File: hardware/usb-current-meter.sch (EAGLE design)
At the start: 28 parts, among them IC2 OPA2234U, U1 ATTINY45, X1 MC2, X3 USB-A-H

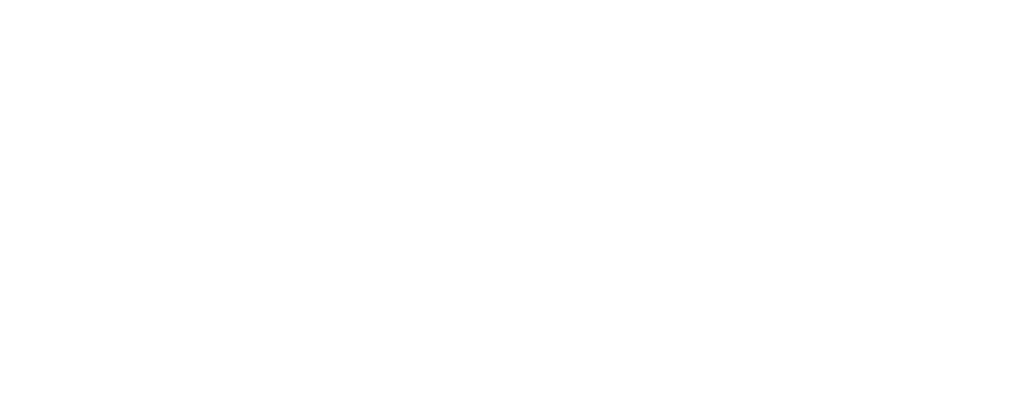
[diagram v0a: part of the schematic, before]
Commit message: hardware: add license, silkscreen
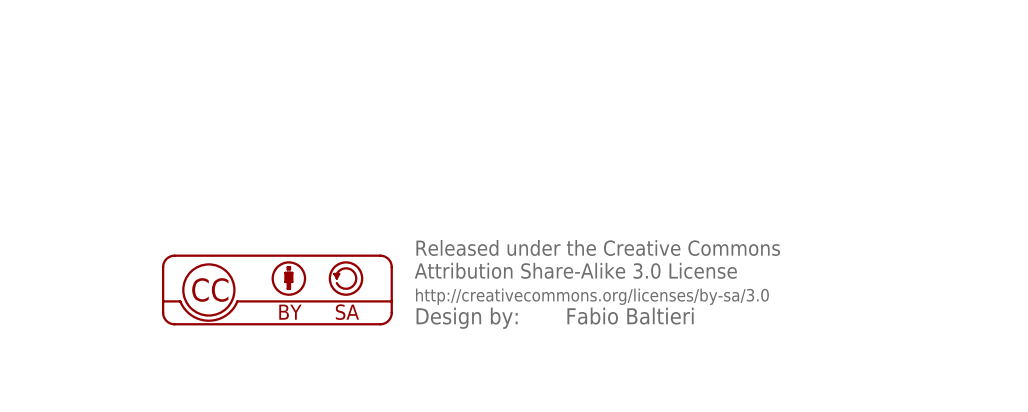
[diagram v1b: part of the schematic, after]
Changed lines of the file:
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@@
 <grid distance="0.1" unitdist="inch" unit="inch" style="lines" multiple="1" display="no" altdistance="0.01" altunitdist="inch" altunit="inch"/>
 <layers>
-<layer number="1" name="Top" color="4" fill="1" visible="yes" active="no"/>
-<layer number="16" name="Bottom" color="1" fill="1" visible="yes" active="no"/>
-<layer number="17" name="Pads" color="2" fill="1" visible="yes" active="no"/>
-<layer number="18" name="Vias" color="2" fill="1" visible="yes" active="no"/>
-<layer number="19" name="Unrouted" color="6" fill="1" visible="yes" active="no"/>
-<layer number="20" name="Dimension" color="15" fill="1" visible="yes" active="no"/>
-<layer number="21" name="tPlace" color="7" fill="1" visible="yes" active="no"/>
-<layer number="22" name="bPlace" color="7" fill="1" visible="yes" active="no"/>
-<layer number="23" name="tOrigins" color="15" fill="1" visible="yes" active="no"/>
-<layer number="24" name="bOrigins" color="15" fill="1" visible="yes" active="no"/>
-<layer number="25" name="tNames" color="7" fill="1" visible="yes" active="no"/>
-<layer number="26" name="bNames" color="7" fill="1" visible="yes" active="no"/>
-<layer number="27" name="tValues" color="7" fill="1" visible="yes" active="no"/>
-<layer number="28" name="bValues" color="7" fill="1" visible="yes" active="no"/>
+<layer number="1" name="Top" color="4" fill="1" visible="no" active="no"/>
+<layer number="16" name="Bottom" color="1" fill="1" visible="no" active="no"/>
+<layer number="17" name="Pads" color="2" fill="1" visible="no" active="no"/>
+<layer number="18" name="Vias" color="2" fill="1" visible="no" active="no"/>
+<layer number="19" name="Unrouted" color="6" fill="1" visible="no" active="no"/>
+<layer number="20" name="Dimension" color="15" fill="1" visible="no" active="no"/>
+<layer number="21" name="tPlace" color="7" fill="1" visible="no" active="no"/>
+<layer number="22" name="bPlace" color="7" fill="1" visible="no" active="no"/>
+<layer number="23" name="tOrigins" color="15" fill="1" visible="no" active="no"/>
+<layer number="24" name="bOrigins" color="15" fill="1" visible="no" active="no"/>
+<layer number="25" name="tNames" color="7" fill="1" visible="no" active="no"/>
+<layer number="26" name="bNames" color="7" fill="1" visible="no" active="no"/>
+<layer number="27" name="tValues" color="7" fill="1" visible="no" active="no"/>
+<layer number="28" name="bValues" color="7" fill="1" visible="no" active="no"/>
 <layer number="29" name="tStop" color="7" fill="3" visible="no" active="no"/>
 <layer number="30" name="bStop" color="7" fill="6" visible="no" active="no"/>
@@
 <layer number="35" name="tGlue" color="7" fill="4" visible="no" active="no"/>
 <layer number="36" name="bGlue" color="7" fill="5" visible="no" active="no"/>
-<layer number="37" name="tTest" color="7" fill="1" visible="yes" active="no"/>
-<layer number="38" name="bTest" color="7" fill="1" visible="yes" active="no"/>
+<layer number="37" name="tTest" color="7" fill="1" visible="no" active="no"/>
+<layer number="38" name="bTest" color="7" fill="1" visible="no" active="no"/>
 <layer number="39" name="tKeepout" color="4" fill="11" visible="no" active="no"/>
 <layer number="40" name="bKeepout" color="1" fill="11" visible="no" active="no"/>
@@
 <layer number="44" name="Drills" color="7" fill="1" visible="no" active="no"/>
 <layer number="45" name="Holes" color="7" fill="1" visible="no" active="no"/>
-<layer number="46" name="Milling" color="3" fill="1" visible="yes" active="no"/>
-<layer number="47" name="Measures" color="7" fill="1" visible="yes" active="no"/>
-<layer number="48" name="Document" color="7" fill="1" visible="yes" active="no"/>
-<layer number="49" name="Reference" color="7" fill="1" visible="yes" active="no"/>
-<layer number="50" name="dxf" color="7" fill="1" visible="yes" active="no"/>
-<layer number="51" name="tDocu" color="7" fill="1" visible="yes" active="no"/>
-<layer number="52" name="bDocu" color="7" fill="1" visible="yes" active="no"/>
-<layer number="53" name="tGND_GNDA" color="7" fill="9" visible="yes" active="no"/>
-<layer number="54" name="bGND_GNDA" color="1" fill="9" visible="yes" active="no"/>
-<layer number="56" name="wert" color="7" fill="1" visible="yes" active="no"/>
+<layer number="46" name="Milling" color="3" fill="1" visible="no" active="no"/>
+<layer number="47" name="Measures" color="7" fill="1" visible="no" active="no"/>
+<layer number="48" name="Document" color="7" fill="1" visible="no" active="no"/>
+<layer number="49" name="Reference" color="7" fill="1" visible="no" active="no"/>
+<layer number="50" name="dxf" color="7" fill="1" visible="no" active="no"/>
+<layer number="51" name="tDocu" color="7" fill="1" visible="no" active="no"/>
+<layer number="52" name="bDocu" color="7" fill="1" visible="no" active="no"/>
+<layer number="53" name="tGND_GNDA" color="7" fill="9" visible="no" active="no"/>
+<layer number="54" name="bGND_GNDA" color="1" fill="9" visible="no" active="no"/>
+<layer number="56" name="wert" color="7" fill="1" visible="no" active="no"/>
 <layer number="91" name="Nets" color="2" fill="1" visible="yes" active="yes"/>
 <layer number="92" name="Busses" color="1" fill="1" visible="yes" active="yes"/>
@@
 </part>
 <part name="GND10" library="supply1" deviceset="GND" device=""/>
+<part name="LICENSE1" library="balto" deviceset="CC_BY-SA" device="" value="Fabio Baltieri"/>
 </parts>
 <sheets>
@@
 <instance part="C4" gate="G$1" x="198.12" y="93.98"/>
 <instance part="GND10" gate="1" x="198.12" y="83.82"/>
+<instance part="LICENSE1" gate="G$1" x="165.1" y="25.4"/>
+<instance part="LICENSE1" gate="G$2" x="193.04" y="25.4"/>
 </instances>
 <busses>

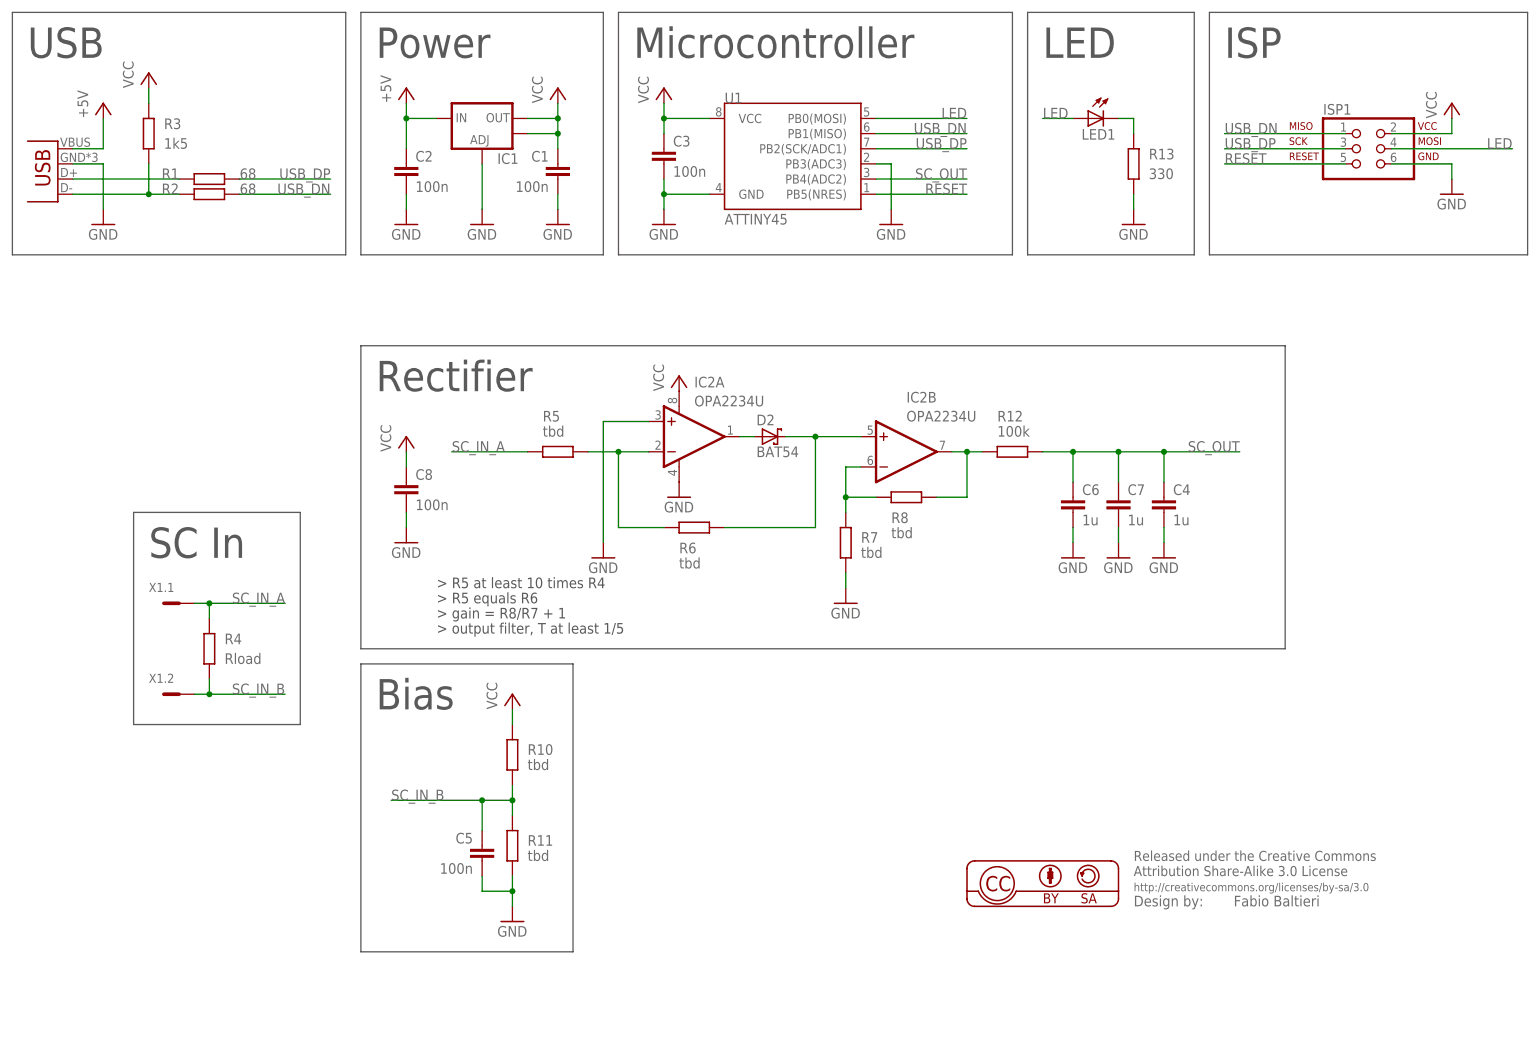
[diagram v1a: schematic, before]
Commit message: hardware: add some filtering capacitors
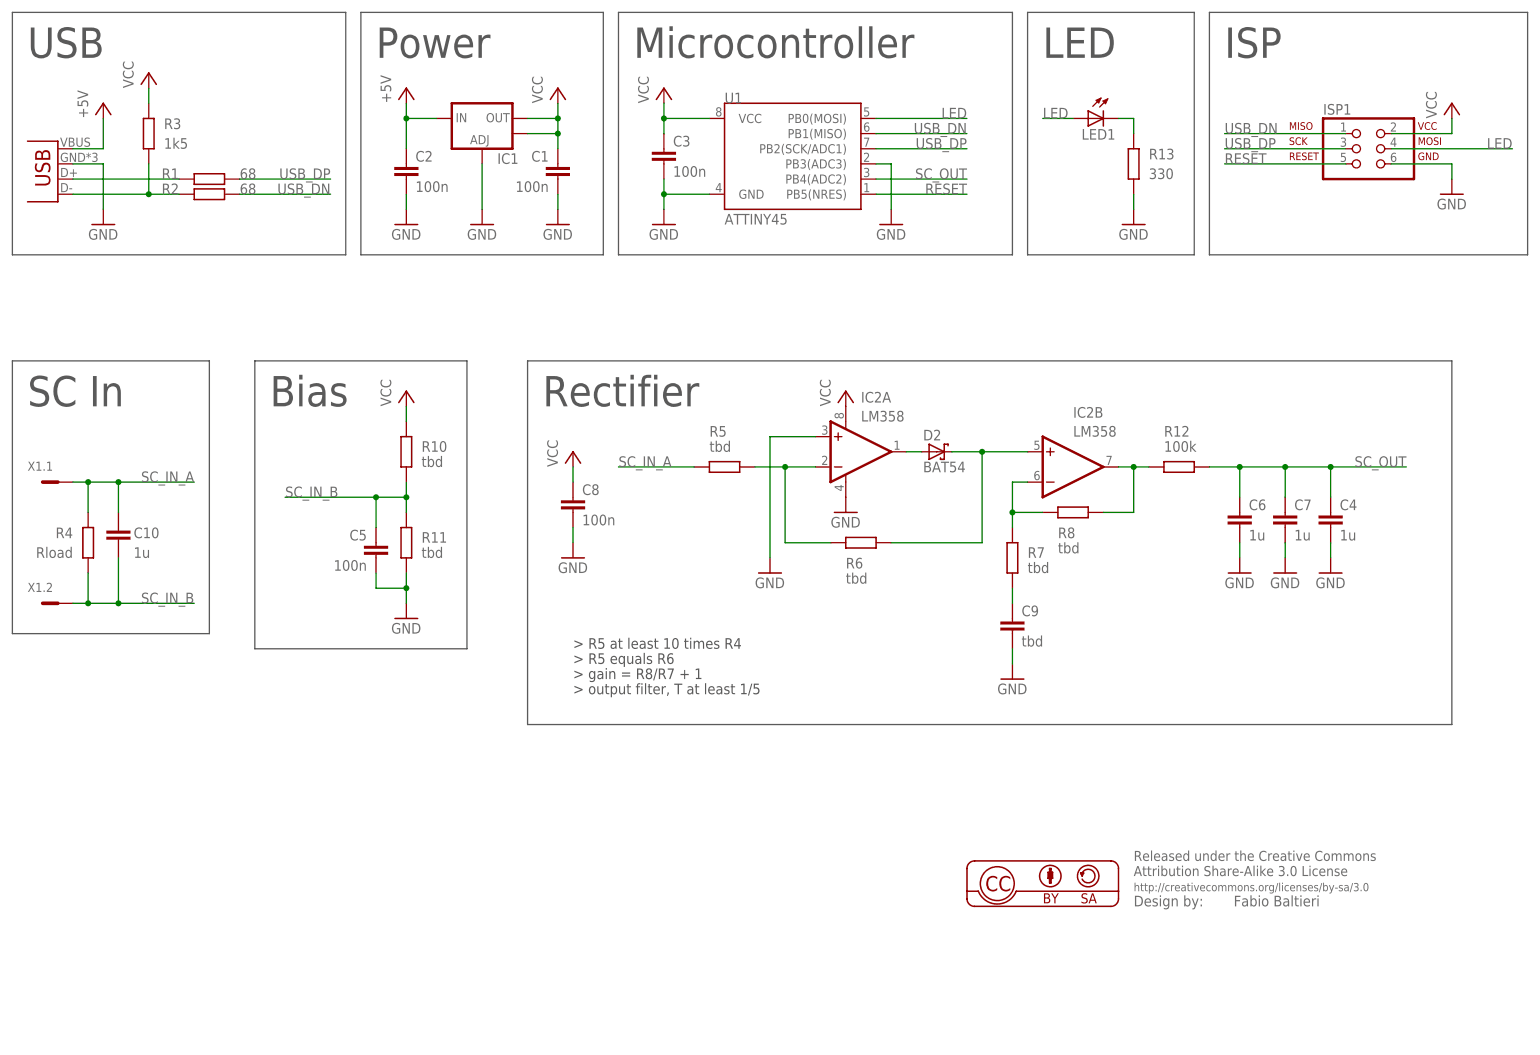
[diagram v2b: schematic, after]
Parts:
- added C10: 1u, rcl:C-EUC0805
- added C9: tbd, rcl:C-EUC0805
- IC2: value OPA2234U -> LM358
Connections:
- new net N$4: C9.1, R7.1
- net GND: now also C9.2; no longer R7.1
- net SC_IN_A: now also C10.1
- net SC_IN_B: now also C10.2
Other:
- moved on the sheet: C4, C5, C6, C7, C8, D2, IC2A, IC2B, R10, R11, R12, R4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
